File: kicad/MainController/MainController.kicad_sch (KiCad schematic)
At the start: 20 parts, among them J1 Controller, J10 Barrel_Jack_Switch, J2 Screen, J3 JTAG, U1 ESP32-WROOM32-DevKit, U2 MAX3232, U3 L7805, U4 LTV-817, U5 LTV-817

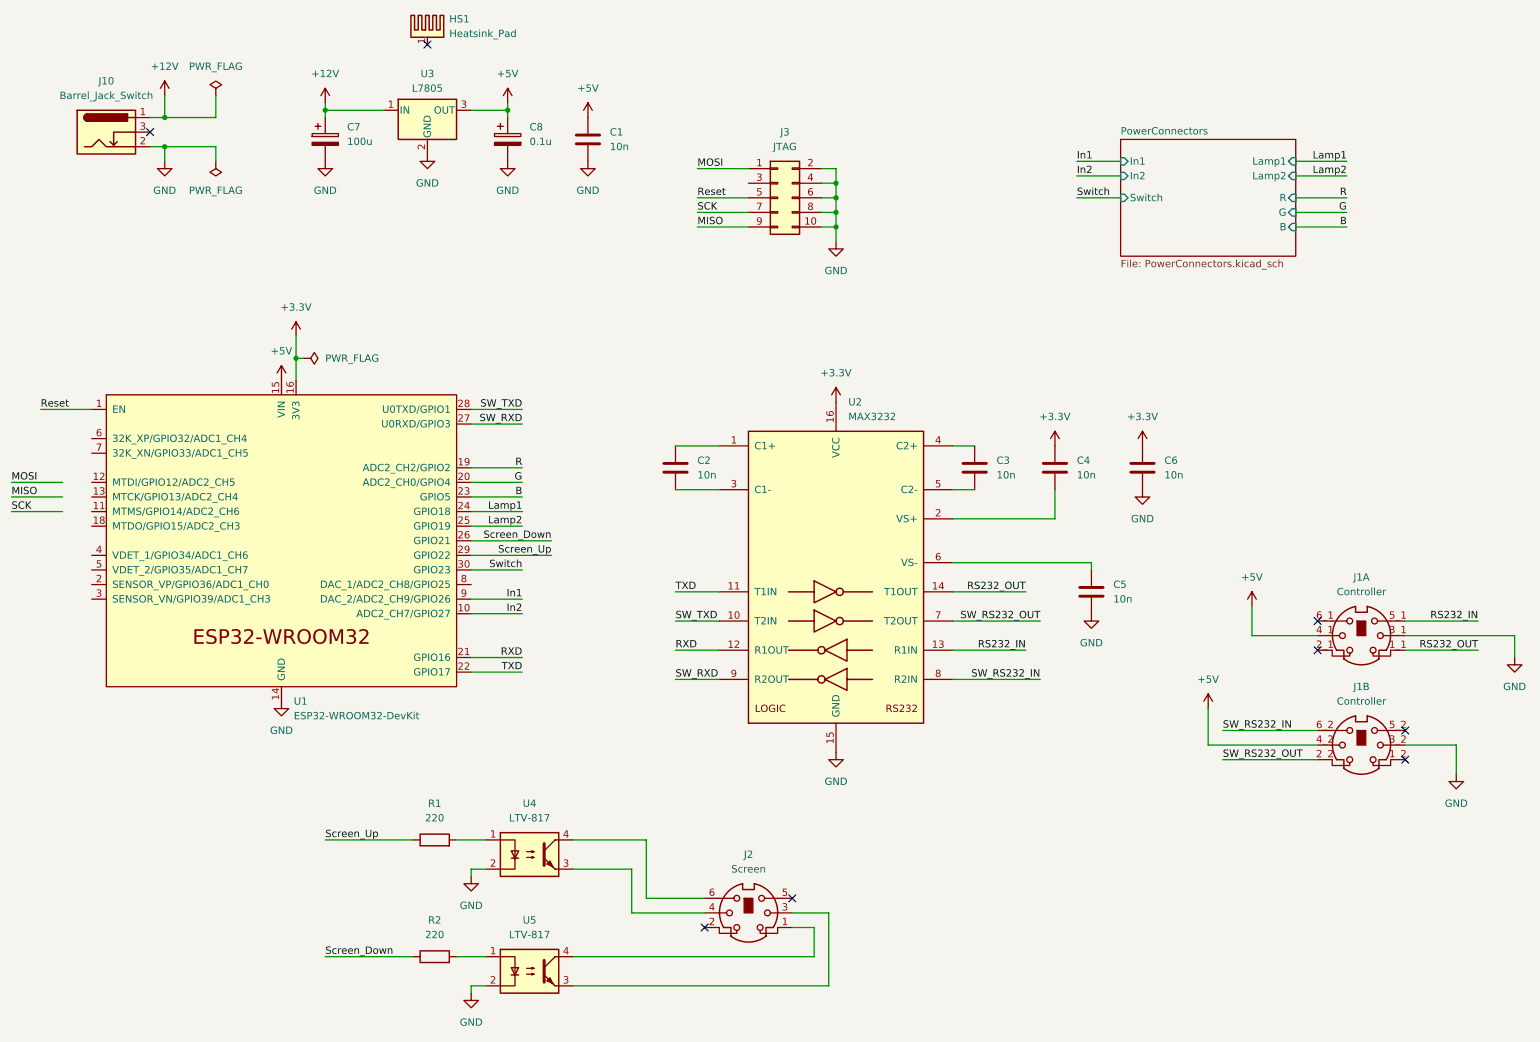
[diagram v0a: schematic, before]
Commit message: New main controller PCB layout using ESP32
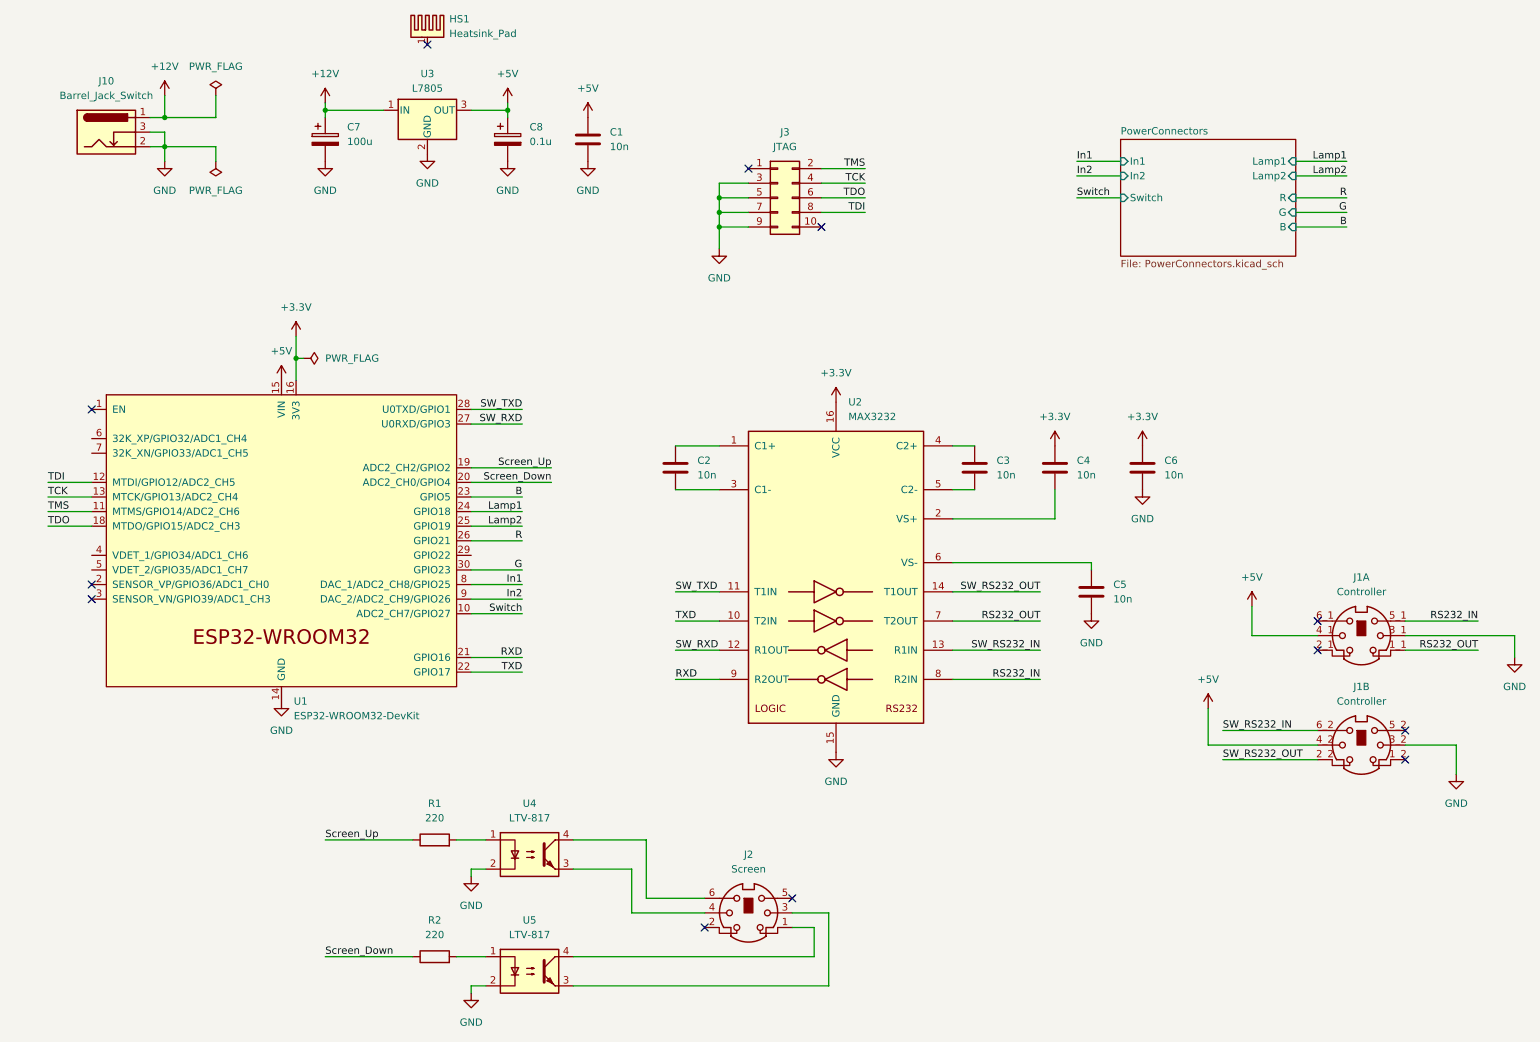
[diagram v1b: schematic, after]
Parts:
- J2: footprint (none) -> SnapEDA:MiniDIN TE_5749180-1
- R1, R2: footprint Resistor_THT:R_Axial_DIN0204_L3.6mm_D1.6mm_P2.54mm_Vertical -> Resistor_THT:R_Axial_DIN0207_L6.3mm_D2.5mm_P10.16mm_Horizontal
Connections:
- net MISO is gone; now on net GND: J3.9 (Pin_9)
- net SCK is gone; now on net GND: J3.7 (Pin_7)
- net G: now also U1.30 (GPIO23); no longer U1.20 (ADC2_CH0/GPIO4)
- net GND: now also J10.3, J3.3 (Pin_3), J3.5 (Pin_5); no longer J3.10 (Pin_10), J3.2 (Pin_2), J3.4 (Pin_4), J3.6 (Pin_6), J3.8 (Pin_8)
- net In1: now also U1.8 (DAC_1/ADC2_CH8/GPIO25); no longer U1.9 (DAC_2/ADC2_CH9/GPIO26)
- net In2: now also U1.9 (DAC_2/ADC2_CH9/GPIO26); no longer U1.10 (ADC2_CH7/GPIO27)
- net R: now also U1.26 (GPIO21); no longer U1.19 (ADC2_CH2/GPIO2)
- net RS232_IN: now also U2.8 (R2IN); no longer U2.13 (R1IN)
- net RS232_OUT: now also U2.7 (T2OUT); no longer U2.14 (T1OUT)
- net RXD: now also U2.9 (R2OUT); no longer U2.12 (R1OUT)
- net SW_RS232_IN: now also U2.13 (R1IN); no longer U2.8 (R2IN)
- net SW_RS232_OUT: now also U2.14 (T1OUT); no longer U2.7 (T2OUT)
- net SW_RXD: now also U2.12 (R1OUT); no longer U2.9 (R2OUT)
- net SW_TXD: now also U2.11 (T1IN); no longer U2.10 (T2IN)
- net Screen_Down: now also U1.20 (ADC2_CH0/GPIO4); no longer U1.26 (GPIO21)
- net Screen_Up: now also U1.19 (ADC2_CH2/GPIO2); no longer U1.29 (GPIO22)
- net Switch: now also U1.10 (ADC2_CH7/GPIO27); no longer U1.30 (GPIO23)
- net TXD: now also U2.10 (T2IN); no longer U2.11 (T1IN)
- net TMS: now reaches U1.11 (MTMS/GPIO14/ADC2_CH6)
- net TMS: now also J3.2 (Pin_2)
- net TDI: now reaches U1.12 (MTDI/GPIO12/ADC2_CH5)
- net TDI: now also J3.8 (Pin_8)
- net TCK: now reaches U1.13 (MTCK/GPIO13/ADC2_CH4)
- net TCK: now also J3.4 (Pin_4)
- net TDO: now reaches U1.18 (MTDO/GPIO15/ADC2_CH3)
- net TDO: now also J3.6 (Pin_6)
- net MOSI: no longer names the net of J3.1 (Pin_1)
- net Reset: no longer names the net of U1.1 (EN)
- net Reset: no longer J3.5 (Pin_5)
- no-connect marks 8 -> 12

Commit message: Updated main controller implementation for ESP32
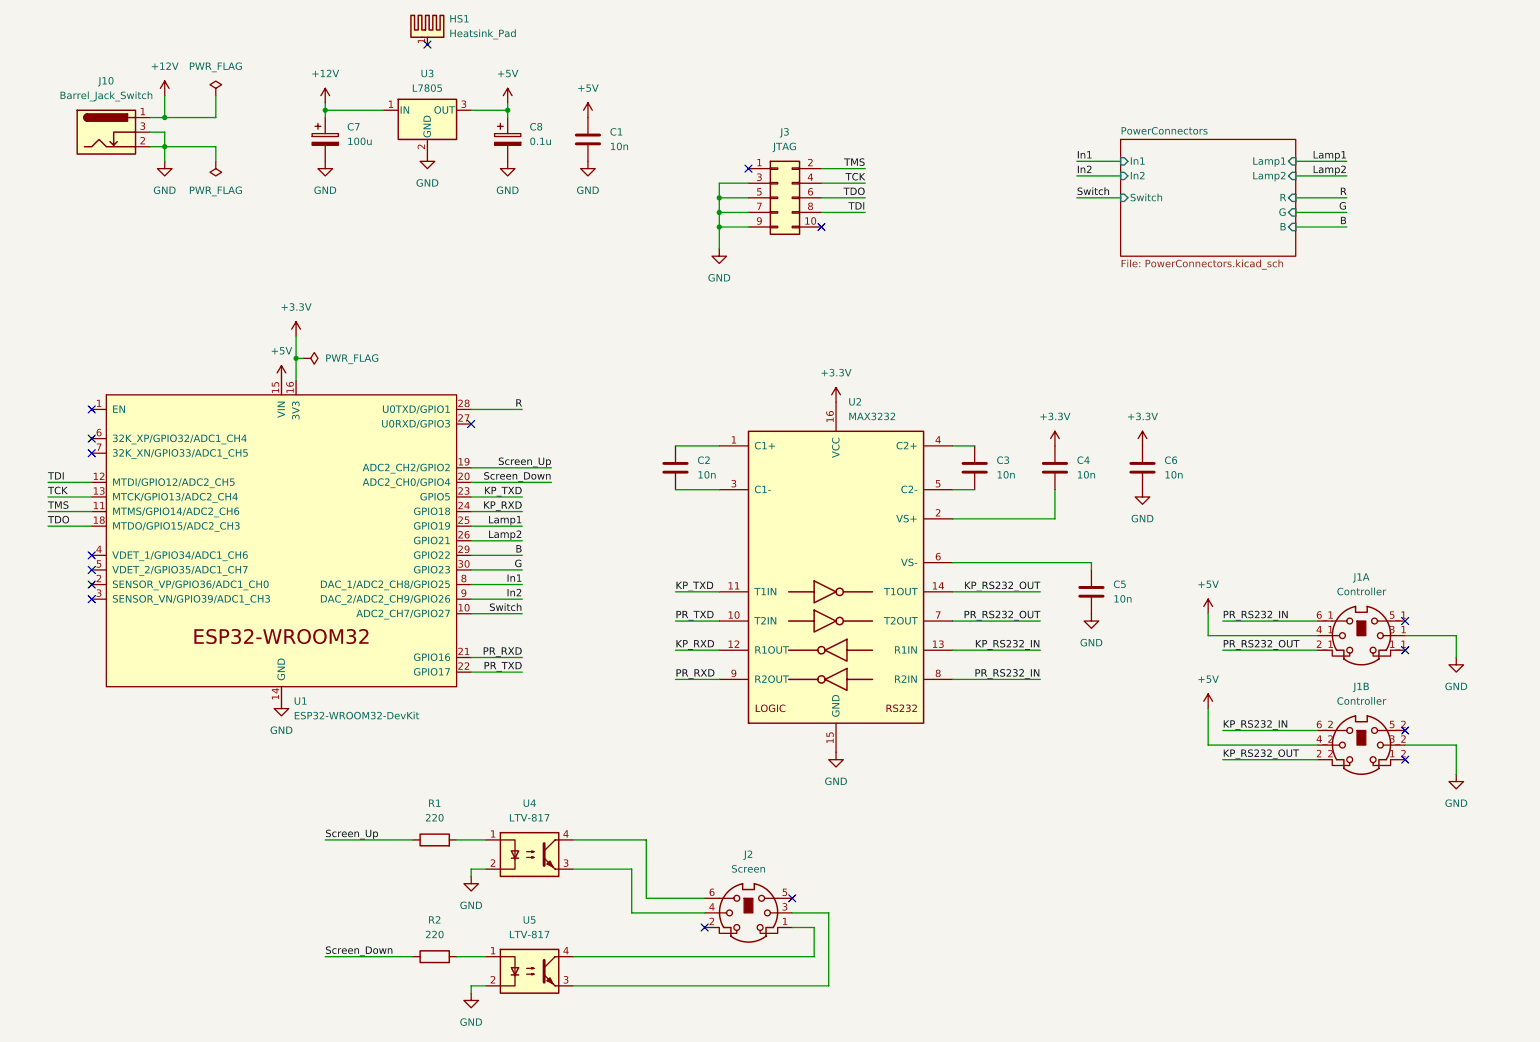
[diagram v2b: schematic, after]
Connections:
- net B: now also U1.29 (GPIO22); no longer U1.23 (GPIO5)
- net Lamp1: now also U1.25 (GPIO19); no longer U1.24 (GPIO18)
- net Lamp2: now also U1.26 (GPIO21); no longer U1.25 (GPIO19)
- net R: now also U1.28 (U0TXD/GPIO1); no longer U1.26 (GPIO21)
- net PR_RS232_OUT: now reaches J1.2_1
- net PR_RS232_OUT: now also U2.7 (T2OUT)
- net PR_RS232_IN: now reaches J1.6_1
- net PR_RS232_IN: now also U2.8 (R2IN)
- net RS232_IN: no longer names the net of J1.5_1
- net RS232_IN: no longer U2.8 (R2IN)
- net RS232_OUT: no longer names the net of J1.1_1
- net RS232_OUT: no longer U2.7 (T2OUT)
- net RXD renamed PR_RXD
- net SW_RS232_IN renamed KP_RS232_IN
- net SW_RS232_OUT renamed KP_RS232_OUT
- net SW_RXD: no longer names the net of U1.27 (U0RXD/GPIO3)
- net SW_RXD: no longer U2.12 (R1OUT)
- net SW_TXD renamed KP_TXD
- net KP_TXD: now also U1.23 (GPIO5); no longer U1.28 (U0TXD/GPIO1)
- net TXD renamed PR_TXD
- new net KP_RXD: U1.24 (GPIO18), U2.12 (R1OUT)
- no-connect marks 12 -> 17
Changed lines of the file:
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@@
 	)
 	(no_connect
-		(at 243.84 127)
+		(at 259.08 127)
+	)
+	(no_connect
+		(at 30.48 110.49)
 	)
 	(no_connect
@@
 	)
 	(no_connect
-		(at 243.84 121.92)
+		(at 259.08 121.92)
+	)
+	(no_connect
+		(at 30.48 113.03)
+	)
+	(no_connect
+		(at 30.48 92.71)
+	)
+	(no_connect
+		(at 30.48 90.17)
 	)
 	(no_connect
@@
 	)
 	(no_connect
+		(at 96.52 87.63)
+	)
+	(no_connect
 		(at 137.16 175.26)
 	)
@@
 	(wire
 		(pts
-			(xy 259.08 124.46) (xy 278.13 124.46)
+			(xy 259.08 124.46) (xy 267.97 124.46)
 		)
 		(stroke
@@
 	(wire
 		(pts
-			(xy 232.41 119.38) (xy 232.41 124.46)
+			(xy 224.79 120.65) (xy 224.79 124.46)
 		)
 		(stroke
@@
 	(wire
 		(pts
-			(xy 259.08 127) (xy 271.78 127)
+			(xy 243.84 127) (xy 227.33 127)
 		)
 		(stroke
@@
 	(wire
 		(pts
-			(xy 96.52 100.33) (xy 105.41 100.33)
+			(xy 96.52 110.49) (xy 105.41 110.49)
 		)
 		(stroke
@@
 	(wire
 		(pts
-			(xy 96.52 102.87) (xy 105.41 102.87)
+			(xy 96.52 105.41) (xy 105.41 105.41)
 		)
 		(stroke
@@
 	(wire
 		(pts
-			(xy 96.52 85.09) (xy 105.41 85.09)
+			(xy 96.52 100.33) (xy 105.41 100.33)
 		)
 		(stroke
@@
 	(wire
 		(pts
-			(xy 278.13 124.46) (xy 278.13 128.27)
+			(xy 267.97 124.46) (xy 267.97 128.27)
 		)
 		(stroke
@@
 	(wire
 		(pts
-			(xy 96.52 87.63) (xy 105.41 87.63)
+			(xy 96.52 102.87) (xy 105.41 102.87)
 		)
 		(stroke
@@
 	(wire
 		(pts
-			(xy 96.52 105.41) (xy 105.41 105.41)
+			(xy 96.52 107.95) (xy 105.41 107.95)
 		)
 		(stroke
@@
 	(wire
 		(pts
-			(xy 232.41 124.46) (xy 243.84 124.46)
+			(xy 224.79 124.46) (xy 243.84 124.46)
 		)
 		(stroke
@@
 	(wire
 		(pts
-			(xy 96.52 107.95) (xy 105.41 107.95)
+			(xy 96.52 85.09) (xy 105.41 85.09)
 		)
 		(stroke
@@
 	(wire
 		(pts
-			(xy 259.08 121.92) (xy 271.78 121.92)
+			(xy 243.84 121.92) (xy 227.33 121.92)
 		)
 		(stroke
@@
 		)
 	)
-	(label "SW_RXD"
-		(at 105.41 87.63 180)
+	(label "KP_RXD"
+		(at 105.41 102.87 180)
 		(effects
 			(font
@@
 		)
 	)
-	(label "RXD"
+	(label "PR_RXD"
 		(at 132.08 132.08 0)
 		(effects
@@
 	)
 	(label "Lamp2"
-		(at 105.41 105.41 180)
+		(at 105.41 107.95 180)
 		(effects
 			(font
@@
 		)
 	)
-	(label "TXD"
+	(label "PR_TXD"
 		(at 105.41 130.81 180)
 		(effects
@@
 		)
 	)
-	(label "SW_RXD"
+	(label "KP_RXD"
 		(at 132.08 127 0)
 		(effects
@@
 		)
 	)
-	(label "TXD"
+	(label "PR_TXD"
 		(at 132.08 121.92 0)
 		(effects
@@
 		)
 	)
-	(label "RS232_IN"
-		(at 271.78 121.92 180)
+	(label "PR_RS232_IN"
+		(at 227.33 121.92 0)
 		(effects
 			(font
 				(size 1.27 1.27)
 			)
-			(justify right bottom)
+			(justify left bottom)
 		)
 	)
-	(label "SW_RS232_IN"
+	(label "KP_RS232_IN"
 		(at 195.58 127 180)
 		(effects
@@
 		)
 	)
-	(label "SW_RS232_OUT"
+	(label "KP_RS232_OUT"
 		(at 195.58 116.84 180)
 		(effects
@@
 		)
 	)
-	(label "RXD"
+	(label "PR_RXD"
 		(at 105.41 128.27 180)
 		(effects
@@
 		)
 	)
-	(label "SW_TXD"
+	(label "KP_TXD"
 		(at 132.08 116.84 0)
 		(effects
@@
 		)
 	)
-	(label "SW_RS232_OUT"
+	(label "KP_RS232_OUT"
 		(at 227.33 146.05 0)
 		(effects
@@
 		)
 	)
-	(label "RS232_OUT"
+	(label "PR_RS232_OUT"
 		(at 195.58 121.92 180)
 		(effects
@@
 		)
 	)
-	(label "RS232_OUT"
-		(at 271.78 127 180)
+	(label "PR_RS232_OUT"
+		(at 227.33 127 0)
 		(effects
 			(font
 				(size 1.27 1.27)
 			)
-			(justify right bottom)
+			(justify left bottom)
 		)
 	)
-	(label "SW_TXD"
-		(at 105.41 85.09 180)
+	(label "KP_TXD"
+		(at 105.41 100.33 180)
 		(effects
 			(font
@@
 		)
 	)
-	(label "SW_RS232_IN"
+	(label "KP_RS232_IN"
 		(at 227.33 140.97 0)
 		(effects
@@
 		)
 	)
-	(label "RS232_IN"
+	(label "PR_RS232_IN"
 		(at 195.58 132.08 180)
 		(effects
@@
 	)
 	(label "R"
-		(at 105.41 107.95 180)
+		(at 105.41 85.09 180)
 		(effects
 			(font
@@
 	)
 	(label "Lamp1"
-		(at 105.41 102.87 180)
+		(at 105.41 105.41 180)
 		(effects
 			(font
@@
 	)
 	(label "B"
-		(at 105.41 100.33 180)
+		(at 105.41 110.49 180)
 		(effects
 			(font
@@
 	(symbol
 		(lib_id "power:+5V")
-		(at 232.41 119.38 0)
+		(at 224.79 120.65 0)
 		(unit 1)
 		(exclude_from_sim no)
@@
 		(fields_autoplaced yes)
 		(property "Reference" "#PWR027"
-			(at 232.41 123.19 0)
+			(at 224.79 124.46 0)
 			(effects
 				(font
@@
 		)
 		(property "Value" "+5V"
-			(at 232.41 114.3 0)
+			(at 224.79 115.57 0)
 			(effects
 				(font
@@
 		)
 		(property "Footprint" ""
-			(at 232.41 119.38 0)
+			(at 224.79 120.65 0)
 			(effects
 				(font
@@
 		)
 		(property "Datasheet" ""
-			(at 232.41 119.38 0)
+			(at 224.79 120.65 0)
 			(effects
 				(font
@@
 		)
 		(property "Description" "Power symbol creates a global label with name \"+5V\""
-			(at 232.41 119.38 0)
+			(at 224.79 120.65 0)
 			(effects
 				(font
@@
 	(symbol
 		(lib_id "power:GND")
-		(at 278.13 128.27 0)
+		(at 267.97 128.27 0)
 		(unit 1)
 		(exclude_from_sim no)
@@
 		(fields_autoplaced yes)
 		(property "Reference" "#PWR025"
-			(at 278.13 134.62 0)
+			(at 267.97 134.62 0)
 			(effects
 				(font
@@
 		)
 		(property "Value" "GND"
-			(at 278.13 133.35 0)
+			(at 267.97 133.35 0)
 			(effects
 				(font
@@
 		)
 		(property "Footprint" ""
-			(at 278.13 128.27 0)
+			(at 267.97 128.27 0)
 			(effects
 				(font
@@
 		)
 		(property "Datasheet" ""
-			(at 278.13 128.27 0)
+			(at 267.97 128.27 0)
 			(effects
 				(font
@@
 		)
 		(property "Description" "Power symbol creates a global label with name \"GND\" , ground"
-			(at 278.13 128.27 0)
+			(at 267.97 128.27 0)
 			(effects
 				(font

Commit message: Updated main controller for digital RGB strip
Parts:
- added R9: 100, Resistor_THT:R_Axial_DIN0207_L6.3mm_D2.5mm_P10.16mm_Horizontal, symbol Device:R
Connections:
- net GND: now also R9.2; no longer J10.2, J10.3
- net B renamed RGB_Data
- net G renamed RGB_PWR
- net R: no longer names the net of U1.28 (U0TXD/GPIO1)
- new net GND2: J10.2, J10.3, R9.1
- no-connect marks 17 -> 18
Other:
- sheet PowerConnectors ports: added RGB_Data, RGB_PWR; removed B, G, R
- moved on the sheet: C1, C7, C8, HS1, J3, U1, U3

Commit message: Fixed footprints for MainController board
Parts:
- C1, C2, C3, C4, C5, C6: value 10n -> 100n
- C8: footprint Capacitor_THT:C_Disc_D7.5mm_W2.5mm_P5.00mm -> Capacitor_THT:CP_Radial_D5.0mm_P2.50mm
- R9: value 100 -> 10
- U2: footprint Package_SO:SOIC-16W_5.3x10.2mm_P1.27mm -> Package_SO:SOIC-16_4.55x10.3mm_P1.27mm
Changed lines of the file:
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@@
 			)
 		)
-		(property "Value" "10n"
+		(property "Value" "100n"
 			(at 135.89 96.5199 0)
 			(effects
@@
 			)
 		)
-		(property "Value" "100"
+		(property "Value" "10"
 			(at 59.69 35.56 90)
 			(effects
@@
 			)
 		)
-		(property "Value" "10n"
+		(property "Value" "100n"
 			(at 217.17 96.5199 0)
 			(effects
@@
 			)
 		)
-		(property "Value" "10n"
+		(property "Value" "100n"
 			(at 201.93 96.5199 0)
 			(effects
@@
 			)
 		)
-		(property "Value" "10n"
+		(property "Value" "100n"
 			(at 208.28 118.1099 0)
 			(effects
@@
 			)
 		)
-		(property "Footprint" "Package_SO:SOIC-16W_5.3x10.2mm_P1.27mm"
+		(property "Footprint" "Package_SO:SOIC-16_4.55x10.3mm_P1.27mm"
 			(at 161.29 140.97 0)
 			(effects
@@
 			)
 		)
-		(property "Value" "10n"
+		(property "Value" "100n"
 			(at 187.96 96.5199 0)
 			(effects
@@
 			)
 		)
-		(property "Value" "10n"
+		(property "Value" "100n"
 			(at 129.54 39.3699 0)
 			(effects
@@
 			)
 		)
-		(property "Footprint" "Capacitor_THT:C_Disc_D7.5mm_W2.5mm_P5.00mm"
+		(property "Footprint" "Capacitor_THT:CP_Radial_D5.0mm_P2.50mm"
 			(at 112.7252 41.91 0)
 			(effects

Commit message: Added commandline interface to main controller
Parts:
- R9: value 10 -> 0
- U2: footprint Package_SO:SOIC-16_4.55x10.3mm_P1.27mm -> Package_SO:SOIC-16_3.9x9.9mm_P1.27mm
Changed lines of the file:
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@@
 			)
 		)
-		(property "Value" "10"
+		(property "Value" "0"
 			(at 59.69 35.56 90)
 			(effects
@@
 			)
 		)
-		(property "Footprint" "Package_SO:SOIC-16_4.55x10.3mm_P1.27mm"
+		(property "Footprint" "Package_SO:SOIC-16_3.9x9.9mm_P1.27mm"
 			(at 161.29 140.97 0)
 			(effects
